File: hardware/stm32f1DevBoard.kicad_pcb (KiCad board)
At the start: 2 copper layers, 105.4 x 62.2 mm, 66 parts, among them J1 USB_2, J2 POWER_JACK, J3 SDCARD, M1 Mounting Hole, M2 Mounting Hole, M3 Mounting Hole, M4 Mounting Hole, P1 JTAG, P2 P20, P3 P20, P4 WIFIDEBUG, Q1 MOSFET-N, U1 STM32F102C6, U2 MRF24WB0MX, U3 LM358, U4 VREG-X-5, U5 VREG-5-3.3, X1 32,768Hz, X2 20MHz

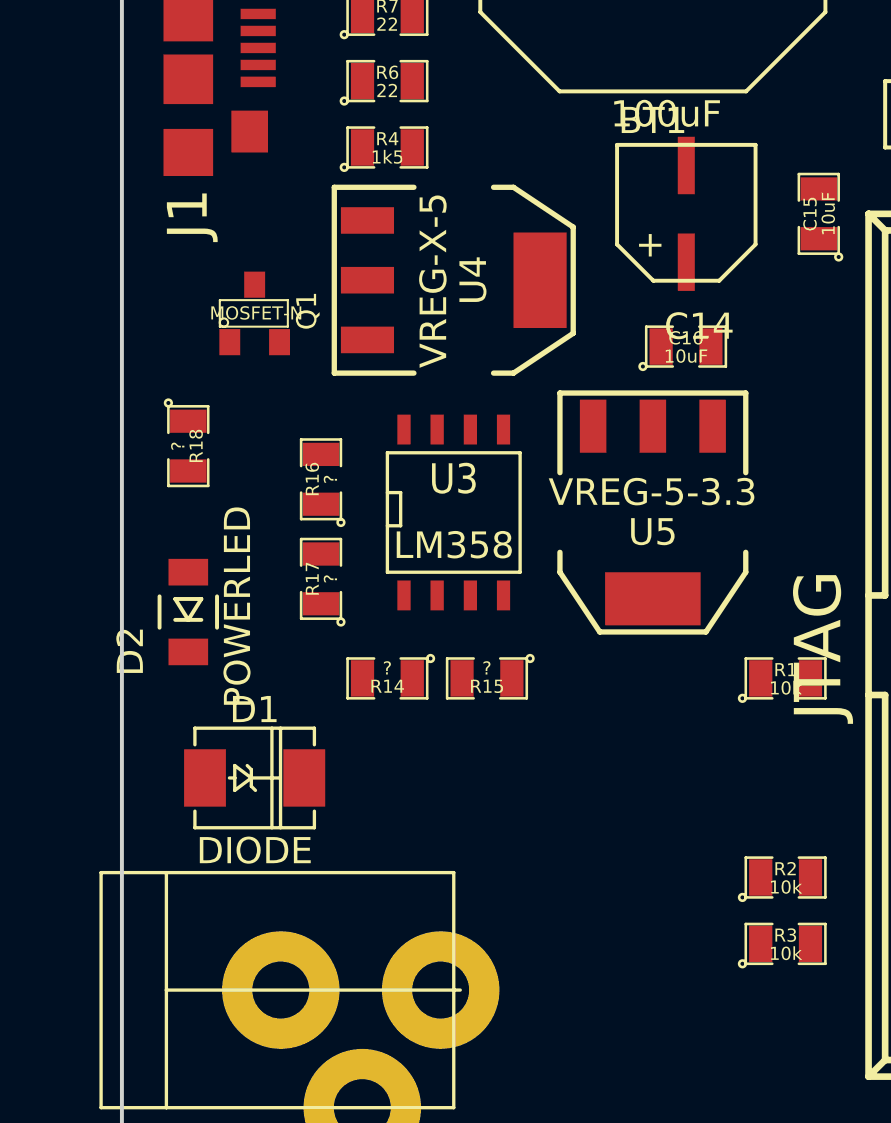
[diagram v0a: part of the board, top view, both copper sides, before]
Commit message: switched transistor
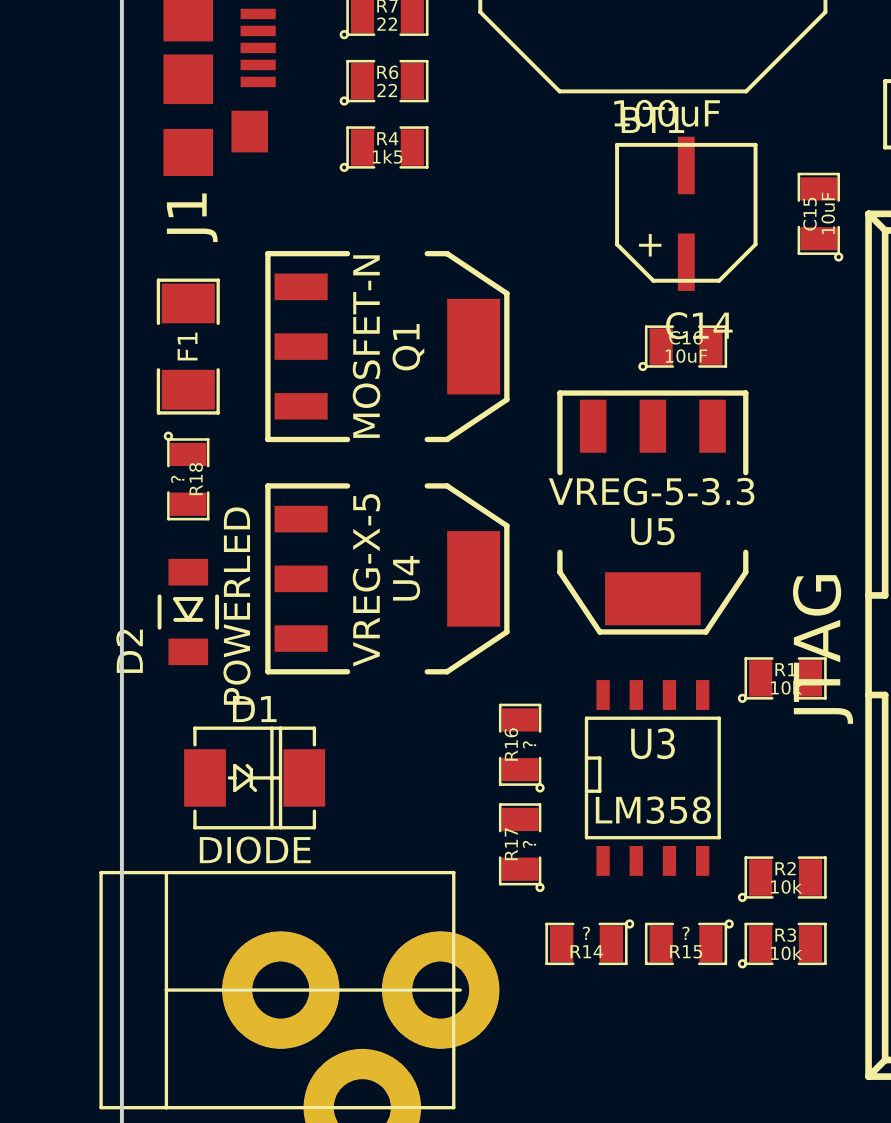
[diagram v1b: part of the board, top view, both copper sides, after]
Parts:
- added F1: FUSE, SM1206, F.Cu at (104.1, 125.7)
- Q1: footprint SOT23 -> SOT223-132
- moved R15 12.7 mm to (123.2, 148.6)
- moved R16 12.7 mm to (116.8, 141.0)
- moved R17 12.7 mm to (116.8, 144.8)
- moved U3 12.7 mm to (121.9, 142.2)
- moved R14 12.7 mm to (119.4, 148.6)
- moved U4 11.7 mm to (111.8, 134.6)
- moved Q1 5.24 mm to (111.8, 125.7), turned to 270 degrees
- moved R18 1.27 mm to (104.1, 130.8)
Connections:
- J1 pad 1: VUSB -> N-0000043

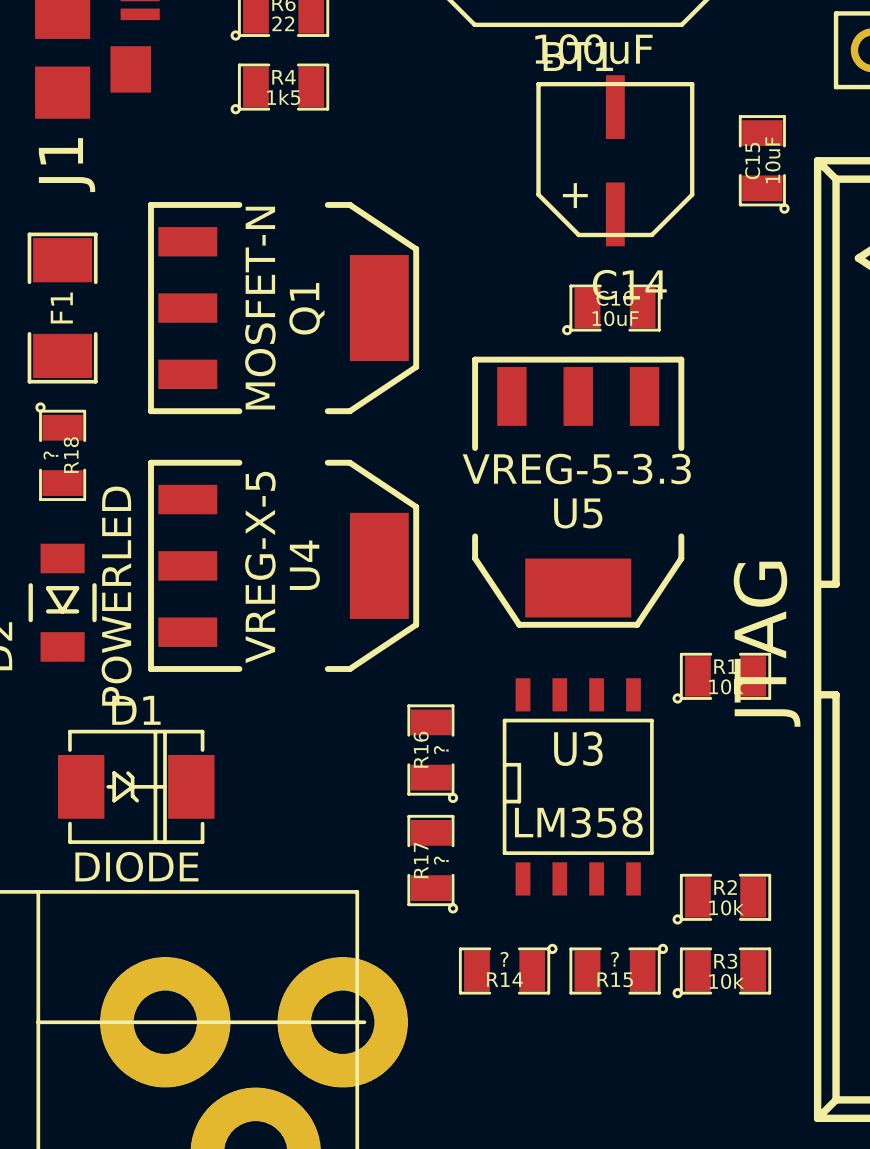
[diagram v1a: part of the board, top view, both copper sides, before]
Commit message: changed to p-ch mosfet
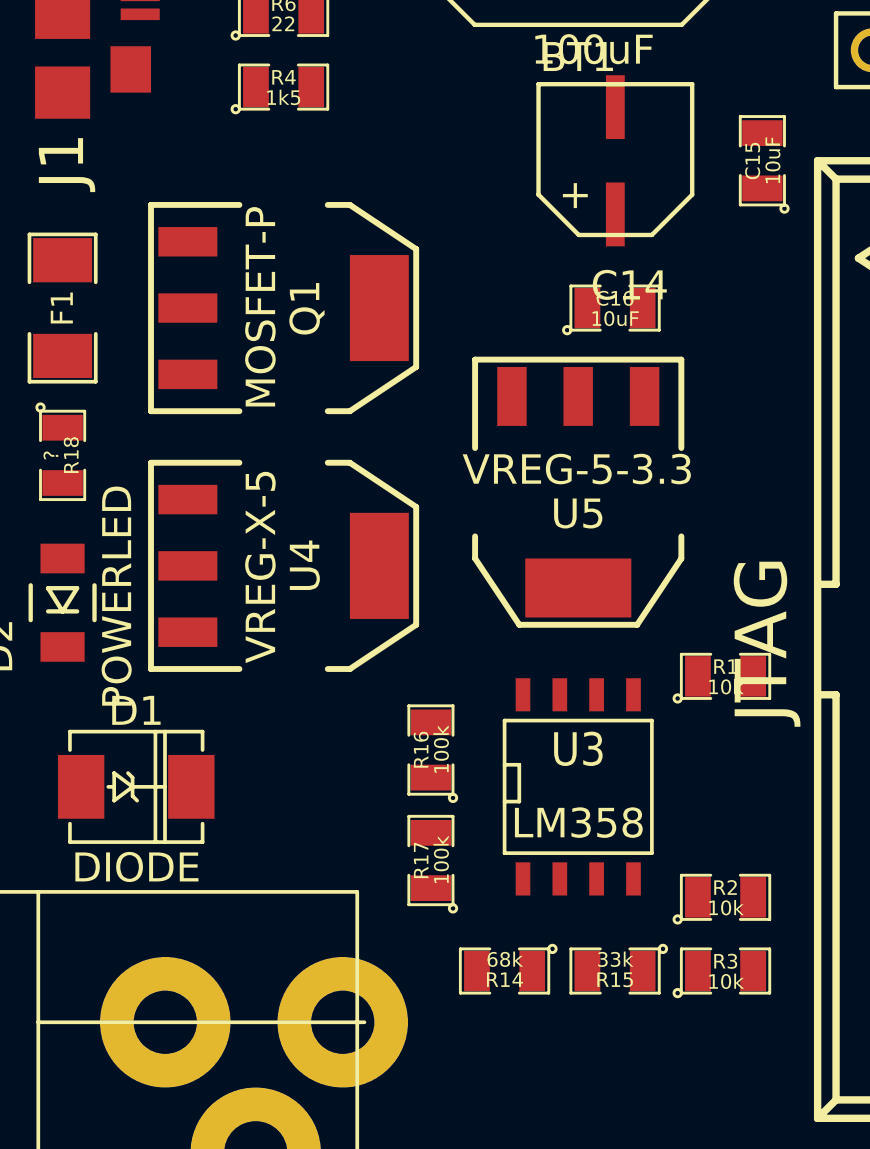
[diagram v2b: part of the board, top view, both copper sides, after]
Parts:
- Q1: value MOSFET-N -> MOSFET-P; footprint SOT223-132 -> SOT223-321
- R14: value ? -> 68k
- R15: value ? -> 33k
- R16, R17: value ? -> 100k

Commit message: layout complete
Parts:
- moved JP1 26.3 mm to (129.2, 130.5), turned to 270 degrees
- moved C7 21.2 mm to (145.7, 128.7)
- moved R11 20.9 mm to (181.0, 114.5)
- moved C12 17.4 mm to (172.9, 117.5)
- moved R9 16.1 mm to (181.0, 116.5)
- moved C1 15.6 mm to (147.8, 109.4), turned to 0 degrees
- moved P2 15.3 mm to (150.8, 148.3), turned to 0 degrees
- moved M3 15.2 mm to (196.5, 146.4)
- moved M1 13.8 mm to (103.8, 146.4)
- moved C9 13.1 mm to (167.9, 114.0)
- moved C8 12.9 mm to (161.0, 127.9), turned to 90 degrees
- moved R5 12.6 mm to (146.7, 143.7), turned to 0 degrees
- moved R10 12.5 mm to (172.9, 119.6), turned to 180 degrees
- moved J2 12.4 mm to (110.2, 137.5)
- moved C15 12.1 mm to (117.1, 115.9)
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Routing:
- net +3.3V: track 0.00 -> 294.5 mm, vias 0 -> 9
- net +5V: track 0.00 -> 146.7 mm
- net nWIFICS: track 0.00 -> 81.2 mm, vias 0 -> 2
- net WIFIHIBERNATE: track 0.00 -> 78.0 mm, vias 0 -> 1
- net MOSI: track 0.00 -> 75.1 mm, vias 0 -> 3
- net nJTRST: track 0.00 -> 74.8 mm, vias 0 -> 4
- net GND: track 0.00 -> 72.5 mm, vias 0 -> 25
- net MISO: track 0.00 -> 71.6 mm, vias 0 -> 5
- net SCK: track 0.00 -> 71.0 mm, vias 0 -> 3
- net nWIFIWP: track 0.00 -> 69.7 mm, vias 0 -> 3
- net nWIFIRESET: track 0.00 -> 57.6 mm, vias 0 -> 2
- net SDCS: track 0.00 -> 50.3 mm
- net N-0000016: track 0.00 -> 50.1 mm, vias 0 -> 2
- net N-0000017: track 0.00 -> 49.5 mm, vias 0 -> 2
- net nRST: track 0.00 -> 49.0 mm, vias 0 -> 1
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- added copper zone on B.Cu, net GND
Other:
- board size 105.4 x 62.2 mm -> 100 x 50 mm
- net class Default: clearance 0.254 -> 0.2032
- rule trace_clearance: 0.254 -> 0.2032

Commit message: labels
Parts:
- moved R5 0.76 mm to (146.7, 142.9)
- moved JP2 0.25 mm to (145.7, 140.4)
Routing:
- net GND: track 72.5 -> 75.4 mm
- net N-0000053: track 26.6 -> 26.0 mm
- net N-0000054: track 3.07 -> 2.57 mm
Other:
- board text added: "3.3V"
- board text added: "5V"
- board text added: "BAT"
- board text added: "BOOT0"
- board text added: "FLASH"
- board text added: "GND"
- board text added: "JTAG EN"
- board text added: "PA0"
- board text added: "PA1"
- board text added: "PA10"
- board text added: "PA13"
- board text added: "PA14"
- board text added: "PA15"
- board text added: "PA2"
- board text added: "PA3"
- board text added: "PA4"
- board text added: "PA5"
- board text added: "PA6"
- board text added: "PA7"
- board text added: "PA8"
- board text added: "PA9"
- board text added: "PB0"
- board text added: "PB1"
- board text added: "PB10"
- board text added: "PB11"
- board text added: "PB12"
- board text added: "PB13"
- board text added: "PB14"
- board text added: "PB15"
- board text added: "PB2"
- board text added: "PB3"
- board text added: "PB4"
- board text added: "PB5"
- board text added: "PB6"
- board text added: "PB7"
- board text added: "PB8"
- board text added: "PB9"
- board text added: "PC13"
- board text added: "RESET"
- board text added: "SYS"
- board text added: "WIFI DBG"
- board text added: "WIFI EN"

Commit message: more board work
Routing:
- net N-0000083: track 14.8 -> 15.4 mm

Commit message: v1
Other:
- board text added: "STM32F1DevBoard Version: 1 By: Joe Ferner Open Source Hardware https://github.com/joeferner/stm32f1DevBoard"
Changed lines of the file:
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@@
     (links 203)
     (no_connects 0)
-    (area 96.142023 96.338519 208.883201 154.398201)
+    (area 96.142023 96.838519 208.883201 154.398201)
     (thickness 1.6)
-    (drawings 50)
+    (drawings 51)
     (tracks 914)
     (zones 0)
@@
   )
   (setup
-    (last_trace_width 0.508)
+    (last_trace_width 0.254)
     (user_trace_width 0.508)
     (trace_clearance 0.2032)
@@
     (pad_to_mask_clearance 0)
     (aux_axis_origin 100 100)
-    (visible_elements FFFFFFBF)
+    (visible_elements FFFF7FBF)
     (pcbplotparams
       (layerselection 15761409)
@@
       (plotreference true)
       (plotvalue false)
-      (plotothertext false)
+      (plotothertext true)
       (plotinvisibletext false)
       (padsonsilk false)
@@
     (at 110.16 137.465 90)
     (attr virtual)
-    (fp_text reference J2 (at 2.8829 2.67462 90) (layer B.SilkS)
+    (fp_text reference J2 (at 3.465 2.84 90) (layer B.SilkS)
       (effects (font (size 1.27 1.27) (thickness 0.0889)))
     )
@@
     (fp_line (start -4.99872 -7.1882) (end -4.99872 3.81) (layer F.SilkS) (width 0.127))
     (fp_text user 3 (at 1.88468 -5.82422 90) (layer B.SilkS)
-      (effects (font (size 1.27 1.27) (thickness 0.0889)))
-    )
-    (fp_text user >NAME (at 3.175 -1.905 180) (layer B.SilkS)
       (effects (font (size 1.27 1.27) (thickness 0.0889)))
     )
@@
     )
   )
+  (gr_text "STM32F1DevBoard\nVersion: 1\nBy: Joe Ferner\nOpen Source Hardware\nhttps://github.com/joeferner/stm32f1DevBoard" (at 193 102) (layer B.SilkS)
+    (effects (font (size 0.75 0.75) (thickness 0.1)) (justify left mirror))
+  )
   (gr_text RESET (at 149.784 136.83 90) (layer F.SilkS)
